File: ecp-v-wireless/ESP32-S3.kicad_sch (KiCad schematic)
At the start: 2 parts, among them U1 ESP32-S3-MINI-1, U2 LFE5U-85F-6BG381x

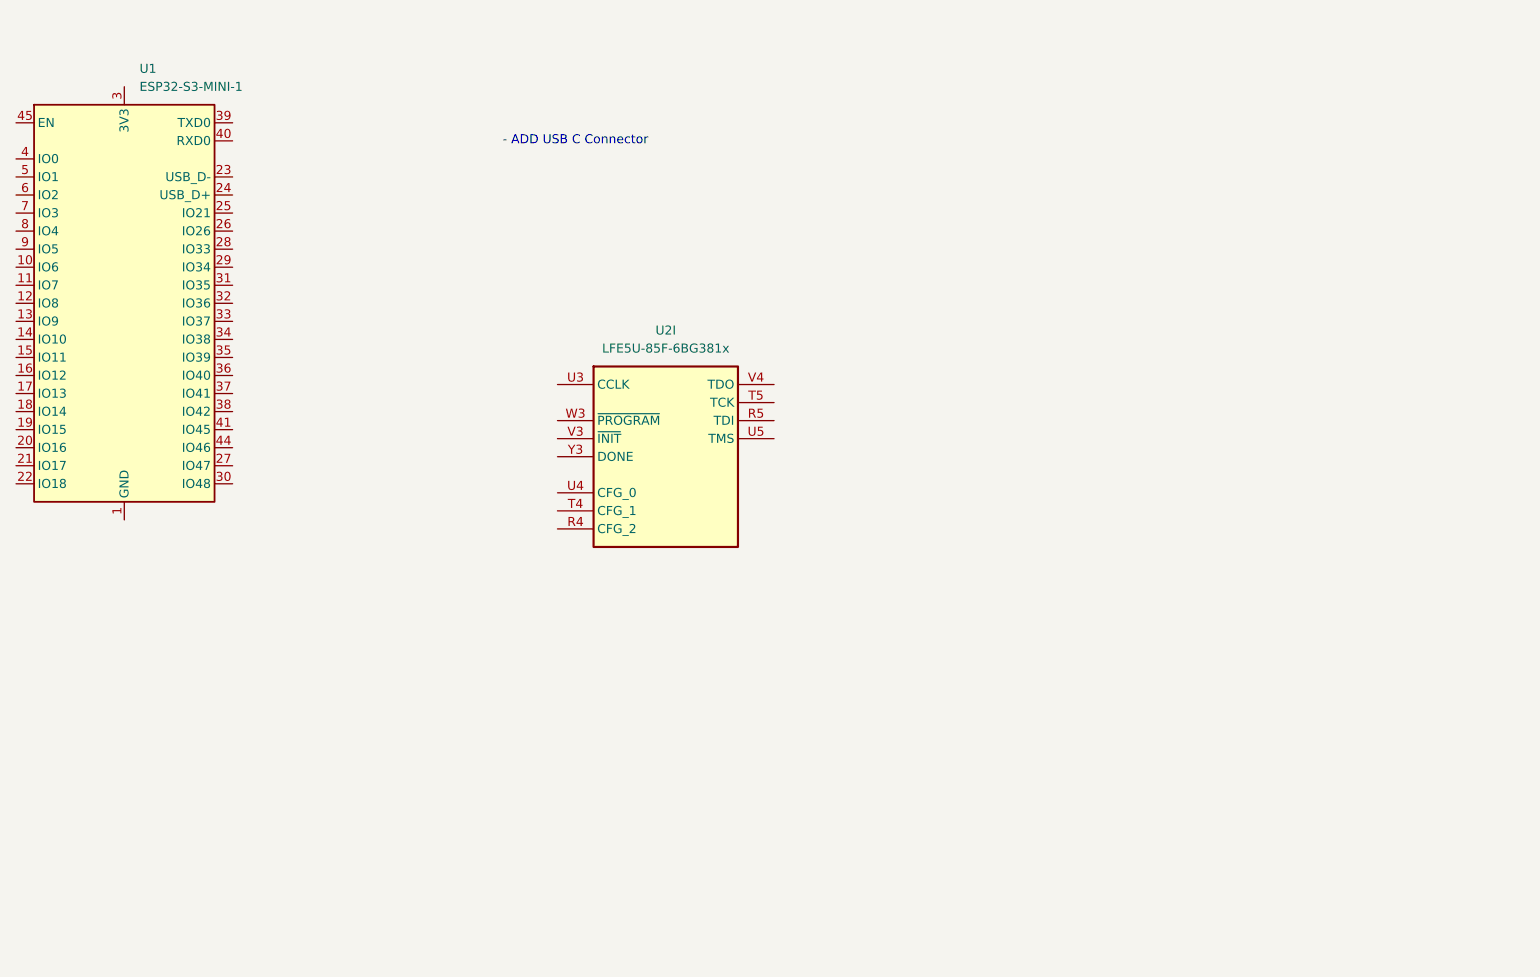
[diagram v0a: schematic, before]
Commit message: Add block diagram, USB, LiPo MGMT, Regs, etc
Signed-off-by: Michael Welling <mwelling79@gmail.com>
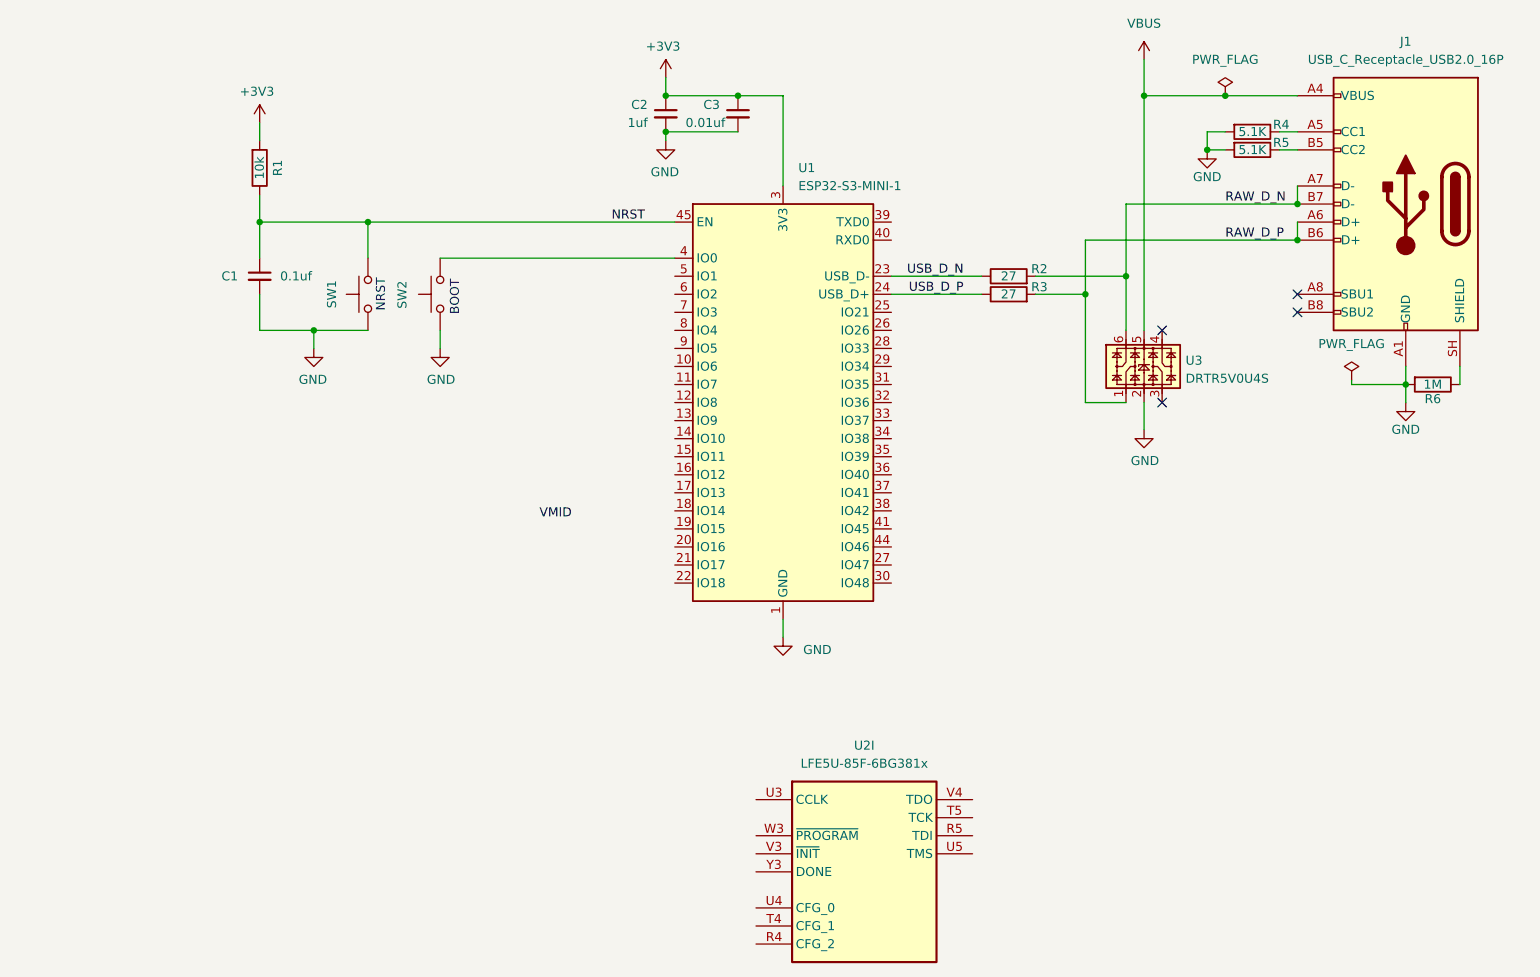
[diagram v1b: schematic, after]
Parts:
- added C1: 0.1uf, Capacitor_SMD:C_0402_1005Metric, symbol Device:C_Small
- added C2: 1uf, Capacitor_SMD:C_0603_1608Metric, symbol Device:C_Small
- added C3: 0.01uf, Capacitor_SMD:C_0603_1608Metric, symbol Device:C_Small
- added J1: USB_C_Receptacle_USB2.0_16P, Connector_USB:USB_C_Receptacle_HRO_TYPE-C-31-M-12, symbol Connector:USB_C_Receptacle_USB2.0_16P
- added R1: 10k, Resistor_SMD:R_0603_1608Metric, symbol Device:R
- added R2, R3: 27, Resistor_SMD:R_0402_1005Metric, symbol Device:R
- added R4, R5: 5.1K, Resistor_SMD:R_0603_1608Metric, symbol Device:R
- added R6: 1M, Resistor_SMD:R_0603_1608Metric, symbol Device:R
- added SW1, SW2: SW_Push, Button_Switch_SMD:SW_SPST_PTS810, symbol Switch:SW_Push
- added U3: DRTR5V0U4S, Package_TO_SOT_SMD:SOT-363_SC-70-6, symbol Power_Protection:NUP4202
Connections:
- net GND: now reaches U1.1 (GND), U1.2 (GND), U1.42 (GND), U1.43 (GND), U1.46 (GND), U1.47 (GND), U1.48 (GND), U1.49 (GND), U1.50 (GND), U1.51 (GND), U1.52 (GND), U1.53 (GND), U1.54 (GND), U1.55 (GND), U1.56 (GND), U1.57 (GND), U1.58 (GND), U1.59 (GND), U1.60 (GND), U1.61 (GND), U1.62 (GND), U1.63 (GND), U1.64 (GND), U1.65 (GND)
- net GND: now also C1.2, C2.2, C3.2, J1.A1 (GND), J1.A12 (GND), J1.B1 (GND), J1.B12 (GND), R4.2, R5.2, R6.2, SW1.1, SW2.1, U3.2
- net USB_D_N: now reaches U1.23 (USB_D-)
- net USB_D_N: now also R2.1
- net USB_D_P: now reaches U1.24 (USB_D+)
- net USB_D_P: now also R3.1
- net +3V3: now reaches U1.3 (3V3)
- net +3V3: now also C2.1, C3.1, R1.2
- net at U1.4 (IO0): now also SW2.2
- net NRST: now reaches U1.45 (EN)
- net NRST: now also C1.1, R1.1, SW1.2
- new net: J1.B5 (CC2), R5.1
- new net: J1.A5 (CC1), R4.1
- new net: J1.SH (SHIELD), R6.1
- new net RAW_D_N: J1.A7 (D-), J1.B7 (D-), R2.2, U3.6
- new net RAW_D_P: J1.A6 (D+), J1.B6 (D+), R3.2, U3.1
- new net VBUS: J1.A4 (VBUS), J1.A9 (VBUS), J1.B4 (VBUS), J1.B9 (VBUS), U3.5
- no-connect marks 0 -> 4
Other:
- note added: "BOOT"
- note added: "NRST"
- note removed: "- ADD USB C Connector"
- moved on the sheet: U1, U2I
